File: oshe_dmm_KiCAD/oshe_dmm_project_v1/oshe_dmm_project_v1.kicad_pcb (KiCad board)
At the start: 4 copper layers, 88.9 x 165.1 mm, 77 parts, among them J1 FTDI Basic, J10 Voltage Range 2, J11 Voltage Range 3, J12 Voltage Range 3, J13 Current, J2 Voltage, J3 GND, J4 Current, J5 USB_C_Receptacle_PowerOnly_6P, J6 ON/OFF, J7 Voltage Range 1, J8 Voltage Range 1, J9 Voltage Range 2, SW1 PTS526 SK15 SMTR2 LFS, U1 ATmega328P-A, U2 INA219BxD, U3 ADS1115IDGS, U4 BQ24075RGT, U5 LM317_SOT-223, Y1 16MHz

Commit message: More PCB changes!
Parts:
- moved D1 0.61 mm to (192.7, 168.5)
- moved R5 0.13 mm to (186.2, 202.1)
- moved REF** 0.07 mm to (199.6, 130.1)
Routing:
- net MISO/D12: track 2.21 -> 103.5 mm
- net MOSI/D11: track 1.99 -> 103.0 mm
- net D5: track 1.97 -> 102.4 mm
- net D2: track 3.53 -> 100.7 mm
- net D3: track 2.78 -> 97.8 mm
- net D4: track 4.69 -> 97.6 mm
- net 2V_Rang: track 53.7 -> 143.8 mm
- net 20V_Rang: track 6.55 -> 79.0 mm
- net Net-(J8-Pin_2): track 3.90 -> 74.8 mm
- net Net-(J10-Pin_2): track 4.79 -> 62.7 mm
- net 200V_Rang: track 6.68 -> 60.9 mm
- net Net-(J12-Pin_2): track 4.05 -> 46.7 mm
- net GND: track 146.3 -> 173.9 mm, vias 27 -> 31
- net +5V: track 88.8 -> 110.9 mm, vias 15 -> 19
- net Input_Negative: track 49.8 -> 67.5 mm
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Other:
- board text added: "DANGER HIGH VOLTAGE"
- board text added: "INSERT QR CODE INSTRUCTIONS HERE"
- board text added: "Open Source Hardware Digital Multimeter Project Version 1 - Spring Semester 2025 Proof of Concept Design DC VOLTAGE AND CURRENT ONLY"

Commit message: Final V1 PCB?!?!?!?
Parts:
- added TP1: SDA, TestPoint:TestPoint_Keystone_5019_Minature, F.Cu at (144.4, 186.6)
- added TP2: SDA, TestPoint:TestPoint_Keystone_5019_Minature, F.Cu at (138.3, 191.2)
- moved R10 7.30 mm to (180.2, 199.3)
- moved R9 7.18 mm to (180.2, 196.8)
- moved C5 6.88 mm to (125.3, 162.0)
- moved C7 6.73 mm to (169.6, 199.9), turned to -90 degrees
- moved J11 5.67 mm to (169.3, 191.4)
- moved J12 5.67 mm to (169.4, 184.2)
- moved J13 5.67 mm to (179.1, 184.2)
- moved J7 5.67 mm to (150.0, 191.4)
- moved J8 5.67 mm to (150.0, 184.2)
- moved R16 5.67 mm to (154.1, 185.2)
- moved R17 5.67 mm to (163.7, 185.2)
- moved R18 5.67 mm to (173.4, 185.2)
- moved R2 5.67 mm to (154.8, 191.4)
- moved R22 5.67 mm to (183.1, 185.1)
- moved R3 5.67 mm to (164.5, 191.4)
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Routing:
- net SCL: track 5.74 -> 89.4 mm, vias 0 -> 4
- net Net-(J13-Pin_2): track 4.03 -> 82.0 mm, vias 1 -> 2
- net SDA: track 4.69 -> 75.8 mm, vias 0 -> 2
- net Input_Negative: track 67.5 -> 83.8 mm
- net V_ADC_Input: track 93.2 -> 83.1 mm
- net Net-(J12-Pin_2): track 46.7 -> 40.2 mm
- net Net-(J10-Pin_2): track 62.7 -> 56.6 mm
- net A3: track 49.1 -> 54.8 mm
- net Net-(J8-Pin_2): track 74.8 -> 69.3 mm
- net 200V_Rang: track 60.9 -> 57.6 mm
- net Net-(U1-XTAL1/PB6): track 16.3 -> 13.1 mm
- net 20V_Rang: track 79.0 -> 76.2 mm
- net +5V: track 110.9 -> 109.0 mm, vias 19 -> 20
- net GND: track 173.9 -> 172.4 mm
- net Net-(U1-XTAL2/PB7): track 11.7 -> 12.8 mm
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- added copper zone on F.Cu, net Net-(D5-A)
- removed copper zone on F.Cu, net Net-(D4-A)
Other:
- outline, holes or cut-outs redrawn
- board text added: "Amp"

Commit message: Updated V1 Board Revision
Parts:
- moved TP2 40.9 mm to (176.7, 205.4), turned to 180 degrees
- moved TP1 2.84 mm to (141.9, 187.9)
- moved D3 2.52 mm to (129.3, 186.7), turned to 180 degrees
- moved R16 2.13 mm to (154.1, 183.1)
- moved R17 2.13 mm to (163.7, 183.1)
- moved R18 2.13 mm to (173.4, 183.1)
- moved R22 2.08 mm to (183.1, 183.1)
- moved R5 1.69 mm to (187.3, 200.8), turned to 180 degrees
- moved R6 1.34 mm to (188.6, 203.4), turned to 180 degrees
- moved R7 1.22 mm to (129.3, 184.0), turned to 0 degrees
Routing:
- net GND: track 172.4 -> 66.8 mm
- net Input_Negative: track 83.8 -> 14.0 mm
- net +5V: track 109.0 -> 52.9 mm, vias 20 -> 21
- net SCL: track 89.4 -> 77.9 mm, vias 4 -> 3
- net A3: track 54.8 -> 46.4 mm
- net Net-(D4-K): track 15.1 -> 17.9 mm
- net Net-(U2-A0): track 2.86 -> 5.30 mm
- net SDA: track 75.8 -> 73.9 mm, vias 2 -> 3
- net Net-(J8-Pin_2): track 69.3 -> 70.3 mm
- net SCK/D13: track 2.36 -> 3.38 mm
- net Net-(J12-Pin_2): track 40.2 -> 41.1 mm
- net Net-(J13-Pin_2): track 82.0 -> 82.8 mm
- added copper zone on F.Cu, net Input_Negative
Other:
- board text added: "SCL"
- board text added: "SDA"

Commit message: updated more stuff
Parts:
- added R3: 330k, Resistor_SMD:R_1206_3216Metric_Pad1.30x1.75mm_HandSolder, F.Cu at (99.1, 180.3)
- added R4: 100k, Resistor_SMD:R_1206_3216Metric_Pad1.30x1.75mm_HandSolder, F.Cu at (99.1, 183.6)
- added R6: 43k, Resistor_SMD:R_1206_3216Metric_Pad1.30x1.75mm_HandSolder, F.Cu at (99.1, 186.9)
- D2: value D_TVS -> VS4V8BU1ART7R
- D5: value 1N4002 -> S1B; footprint Diode_SMD:D_1206_3216Metric_Pad1.42x1.75mm_HandSolder -> Diode_SMD:D_SMA
- R10: renamed from R7; value 330 -> 390
- R14: renamed from R11; value 220K -> 390
- R2: value 900K -> 470k
- R22: renamed from R16; value 1k -> 390
- R24: renamed from R18; value 1k -> 1.78k
- R25: renamed from R22; value 1k -> 3.3k
- R5: renamed from R3; value 90k -> 47k
- moved R19 2.68 mm to (164.9, 212.0)
- moved C12 2.52 mm to (164.9, 209.5)
- moved D5 1.50 mm to (162.8, 217.1)
- moved C13 0.84 mm to (165.3, 223.6)
- moved C10 0.83 mm to (157.0, 208.1)
- moved 5V1 0.81 mm to (150.6, 222.2)
- moved JP2 0.81 mm to (151.5, 215.9)
- moved U5 0.81 mm to (157.0, 218.1)
- moved R20 0.74 mm to (158.6, 212.3)
- renumbered C3 to C2, C2 to C3, R8 to R11, R9 to R12, R10 to R13, R12 to R15, R13 to R16, R14 to R17, R15 to R18, R17 to R23, R4 to R7, R5 to R8, R6 to R9
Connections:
- R2 pad 2: 20V_Rang -> Net-(R2-Pad2)
- R5 pad 2: 200V_Rang -> Net-(R5-Pad2)
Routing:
- net Net-(J6-Pin_2): track 7.41 -> 6.74 mm
- net +5V: vias 21 -> 20

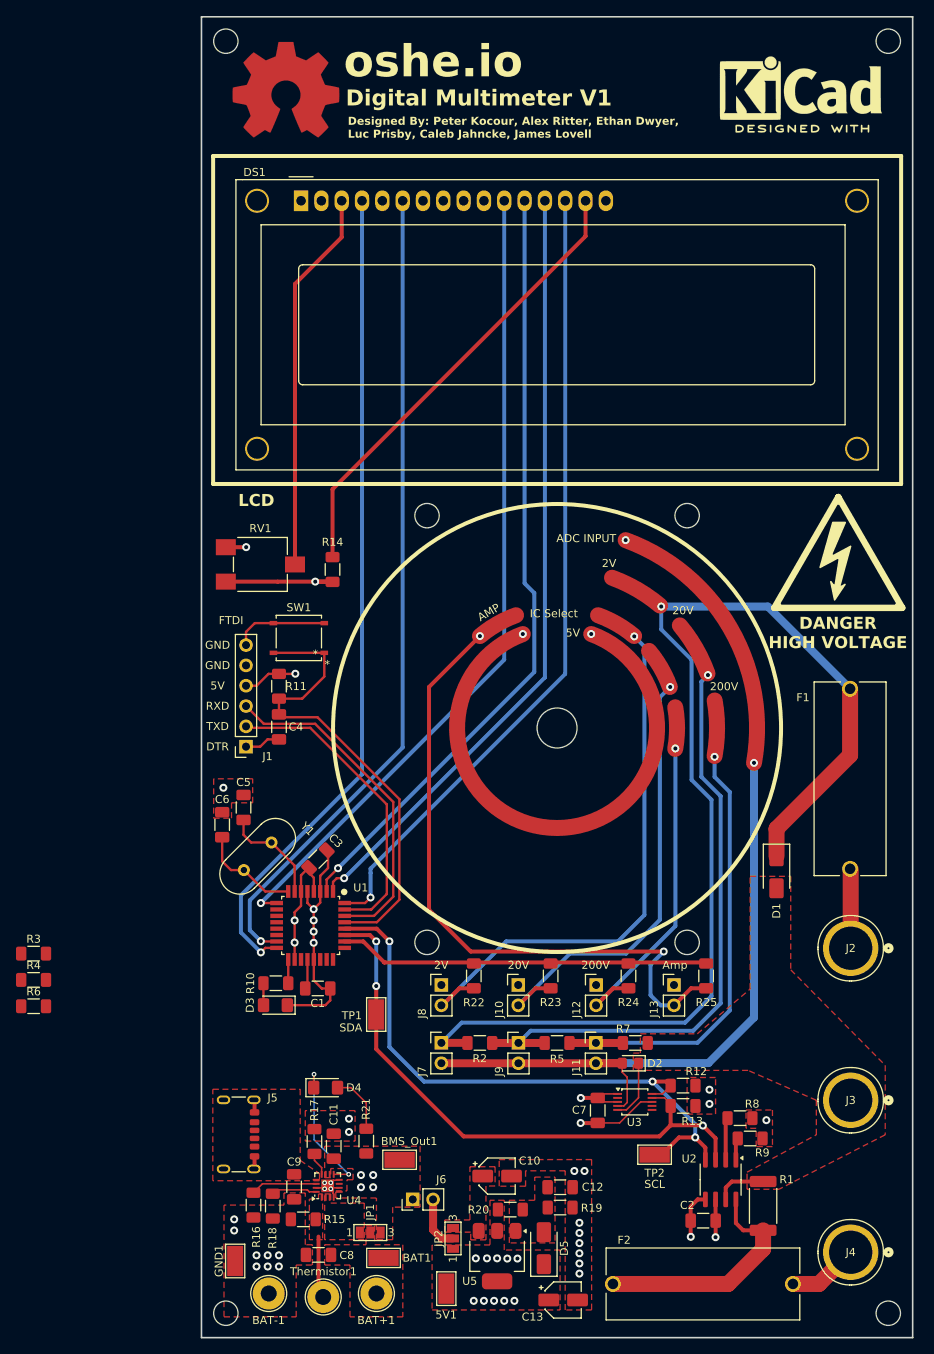
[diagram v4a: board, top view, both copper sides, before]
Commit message: Final Board complete + BOM
Final board design is complete and ready to order. Bill of Materials has also been completed.
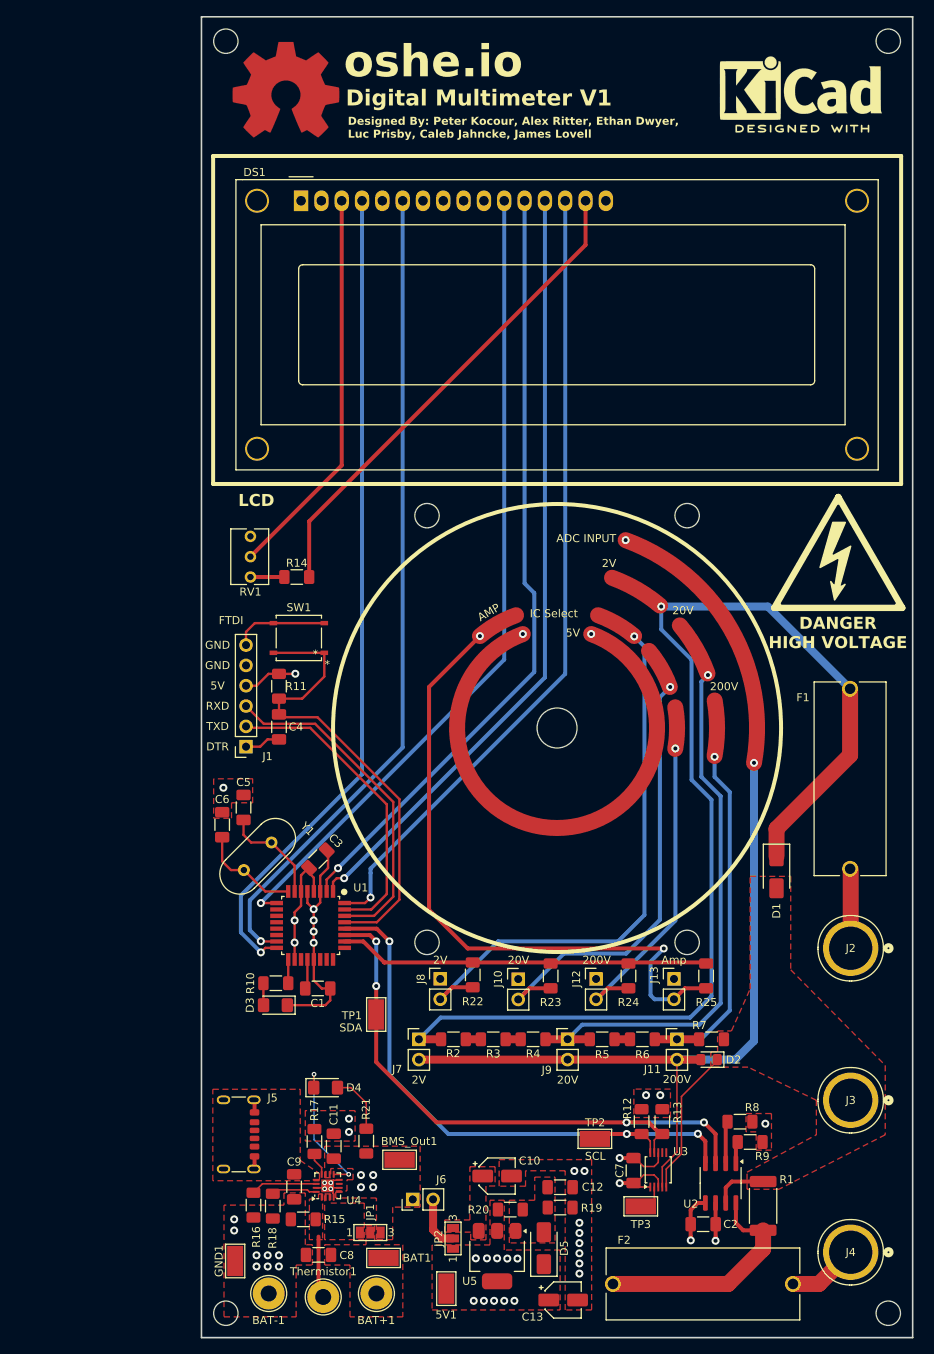
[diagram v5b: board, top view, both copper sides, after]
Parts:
- added TP3: ALERT, TestPoint:TestPoint_Keystone_5019_Minature, F.Cu at (175.0, 211.9)
- J13: value Current -> Current Indication
- R1: value 0.064 -> 0.05
- RV1: value 10k -> 10k - Pot; footprint Potentiometer_SMD:Potentiometer_ACP_CA6-VSMD_Vertical -> Potentiometer_THT:Potentiometer_Bourns_3266Y_Vertical
- moved R6 76.2 mm to (175.2, 191.0)
- moved R4 62.9 mm to (161.5, 191.0)
- moved R3 58.4 mm to (156.5, 191.0)
- moved J11 10.1 mm to (179.5, 191.0)
- moved D2 9.84 mm to (183.5, 193.5)
- moved R7 9.54 mm to (183.8, 191.0)
- moved U3 8.98 mm to (177.1, 207.3), turned to 90 degrees
- moved C7 8.75 mm to (174.0, 207.4), turned to 90 degrees
- moved TP2 7.73 mm to (169.2, 203.4)
- moved R12 6.86 mm to (175.1, 201.3), turned to -90 degrees
- moved J9 6.16 mm to (165.8, 191.0)
- moved R5 5.66 mm to (170.1, 191.0)
- moved R14 4.57 mm to (132.0, 133.2), turned to 0 degrees
- moved R2 3.33 mm to (151.5, 191.0)
- moved R13 3.25 mm to (177.6, 201.3), turned to -90 degrees
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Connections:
- U3 pad 2: unconnected-(U3-ALERT/RDY-Pad2) -> Net-(U3-ALERT/RDY)
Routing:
- net V_ADC_Input: track 83.1 -> 97.3 mm
- net +5V: track 52.9 -> 38.8 mm, vias 20 -> 19
- net 200V_Rang: track 57.6 -> 46.1 mm
- net Input_Negative: track 14.0 -> 25.5 mm
- net 20V_Rang: track 76.2 -> 68.9 mm
- net Net-(U3-ALERT/RDY): track 0.00 -> 4.10 mm
- net Net-(DS1-LED(+)): track 57.6 -> 61.3 mm
- net SDA: track 73.9 -> 76.9 mm, vias 3 -> 4
- net 2V_Rang: track 143.4 -> 145.5 mm
- net Net-(R5-Pad2): track 0.00 -> 1.93 mm
- net Net-(R3-Pad2): track 0.00 -> 1.88 mm
- net Net-(R2-Pad2): track 0.00 -> 1.88 mm
- net Net-(DS1-VO): track 47.9 -> 49.2 mm
- net Net-(J12-Pin_2): track 41.1 -> 40.1 mm
- net Net-(J10-Pin_2): track 56.7 -> 56.1 mm
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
